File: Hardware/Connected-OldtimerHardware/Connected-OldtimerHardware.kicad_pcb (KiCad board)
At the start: 2 copper layers, 26 parts, among them J1 NextionConnector, J2 MainConnector, J3 CAN_Bus_Connector, J4 AUXConnector, Q1 2N3906, U1 ParticleElectron, U2 TSR_2-2450, U3 CANTranceiverModule, U4 AdafruitFRAM, U5 AdafruitUltimateGPS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

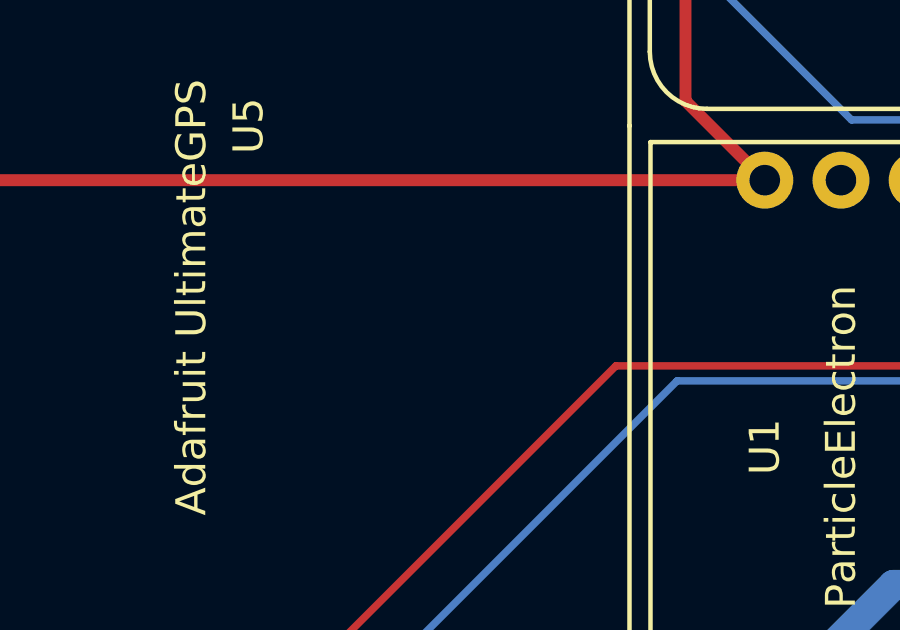
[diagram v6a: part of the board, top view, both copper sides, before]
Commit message: camper silkscreen
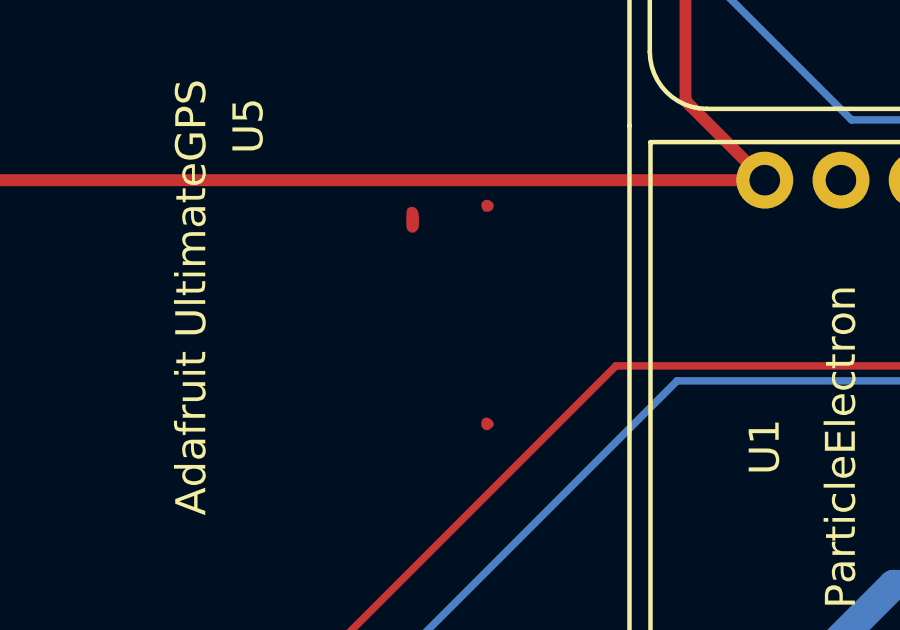
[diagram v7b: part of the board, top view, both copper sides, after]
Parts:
- added G***: LOGO, drawings:smallCamperWifi, F.Cu at (106.7, 81.3)

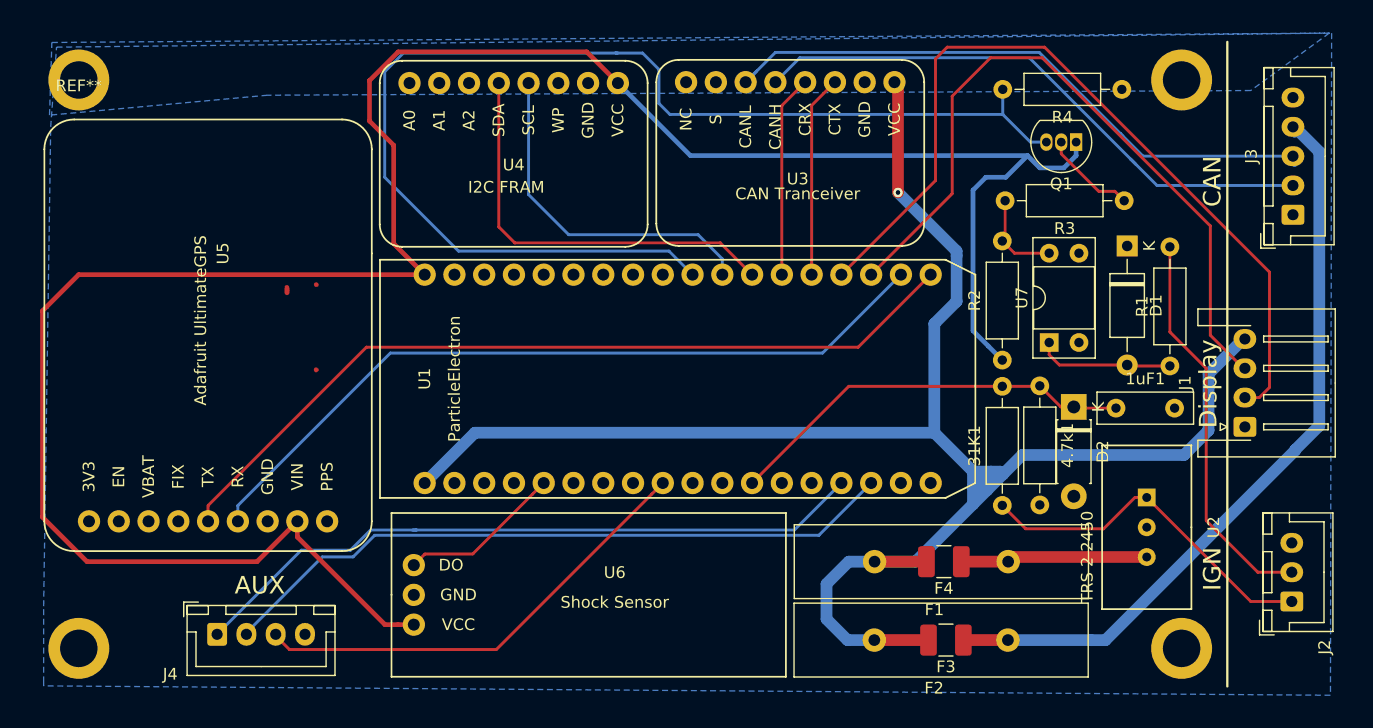
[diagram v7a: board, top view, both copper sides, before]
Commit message: made dem tracks thick
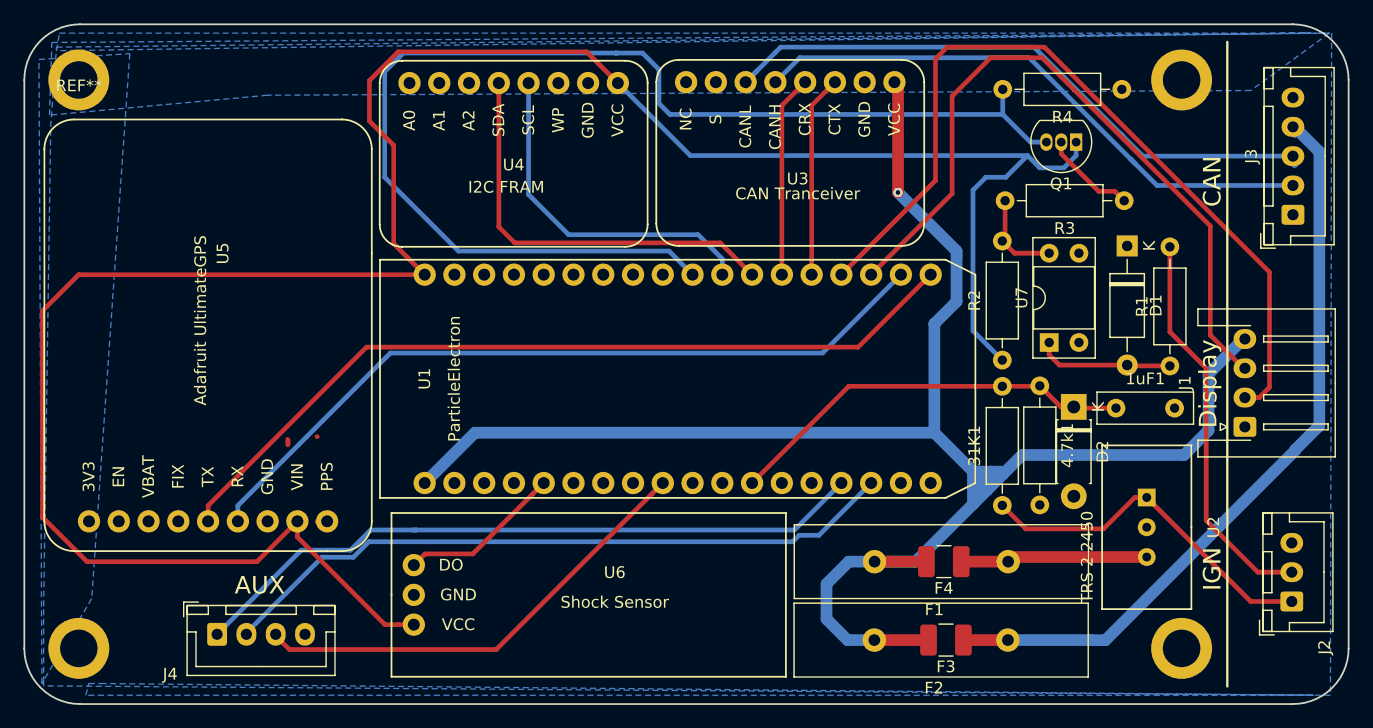
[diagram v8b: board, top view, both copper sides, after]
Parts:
- moved G*** 13.0 mm to (106.8, 94.2)
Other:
- board outline added: 113 x 58 mm
- net class thicko removed
- board text added: "Connected Oldtimer"
- board text added: "Designed in Germany"
- board text added: "Heath Lee"
- board text added: "V 1.0"
